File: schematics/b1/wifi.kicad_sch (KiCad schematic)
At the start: 13 parts, among them J1 SERIAL, SW1 JUMP, SW2 RESET, SW3 BOOT, U1 L7805, U2 ESP-12F

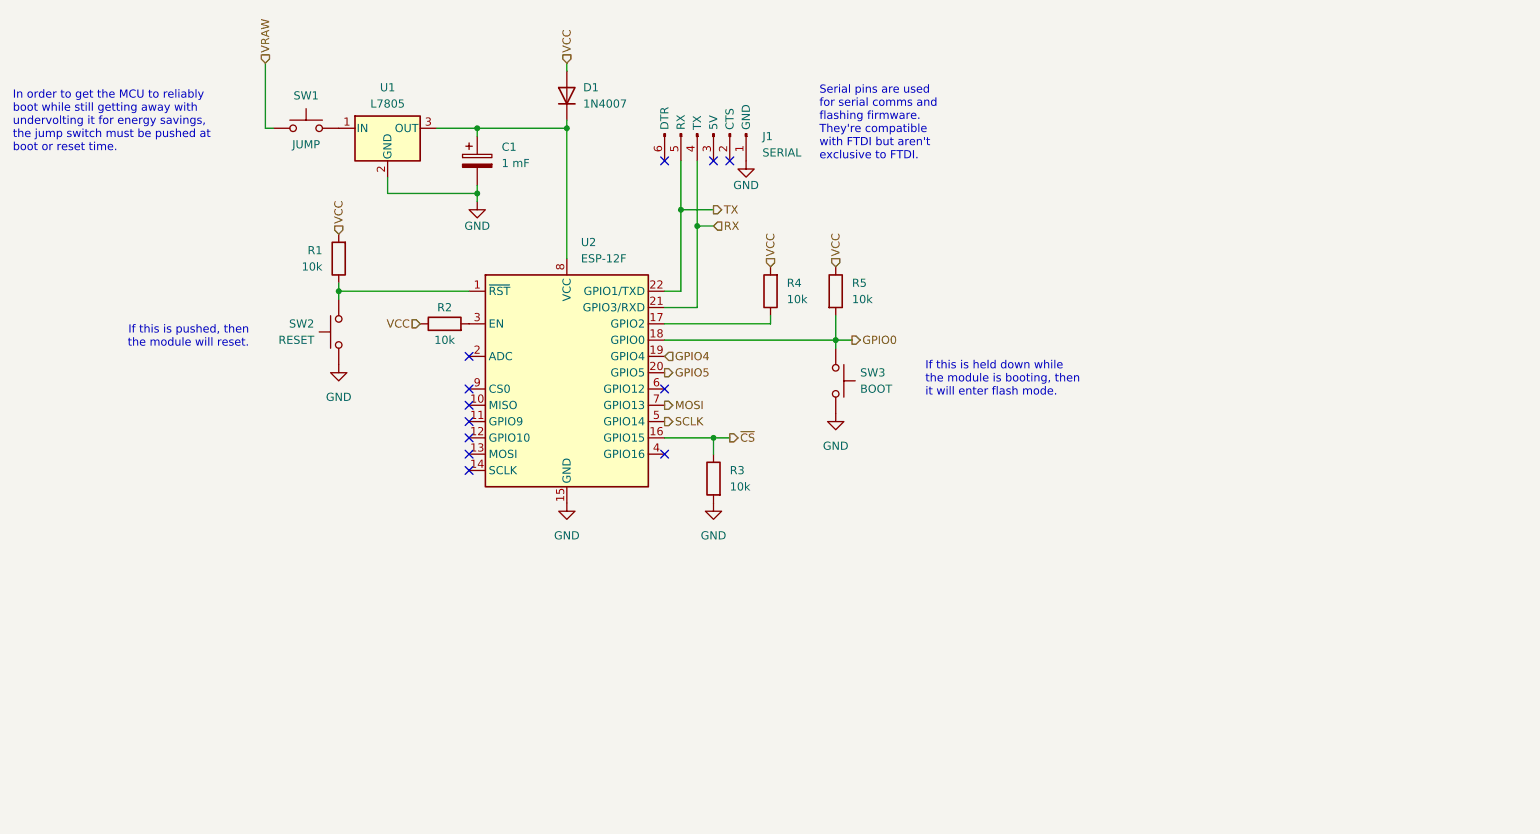
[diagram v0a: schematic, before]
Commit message: Added an MCP23017 IC to the Wi-Fi and MCU block.
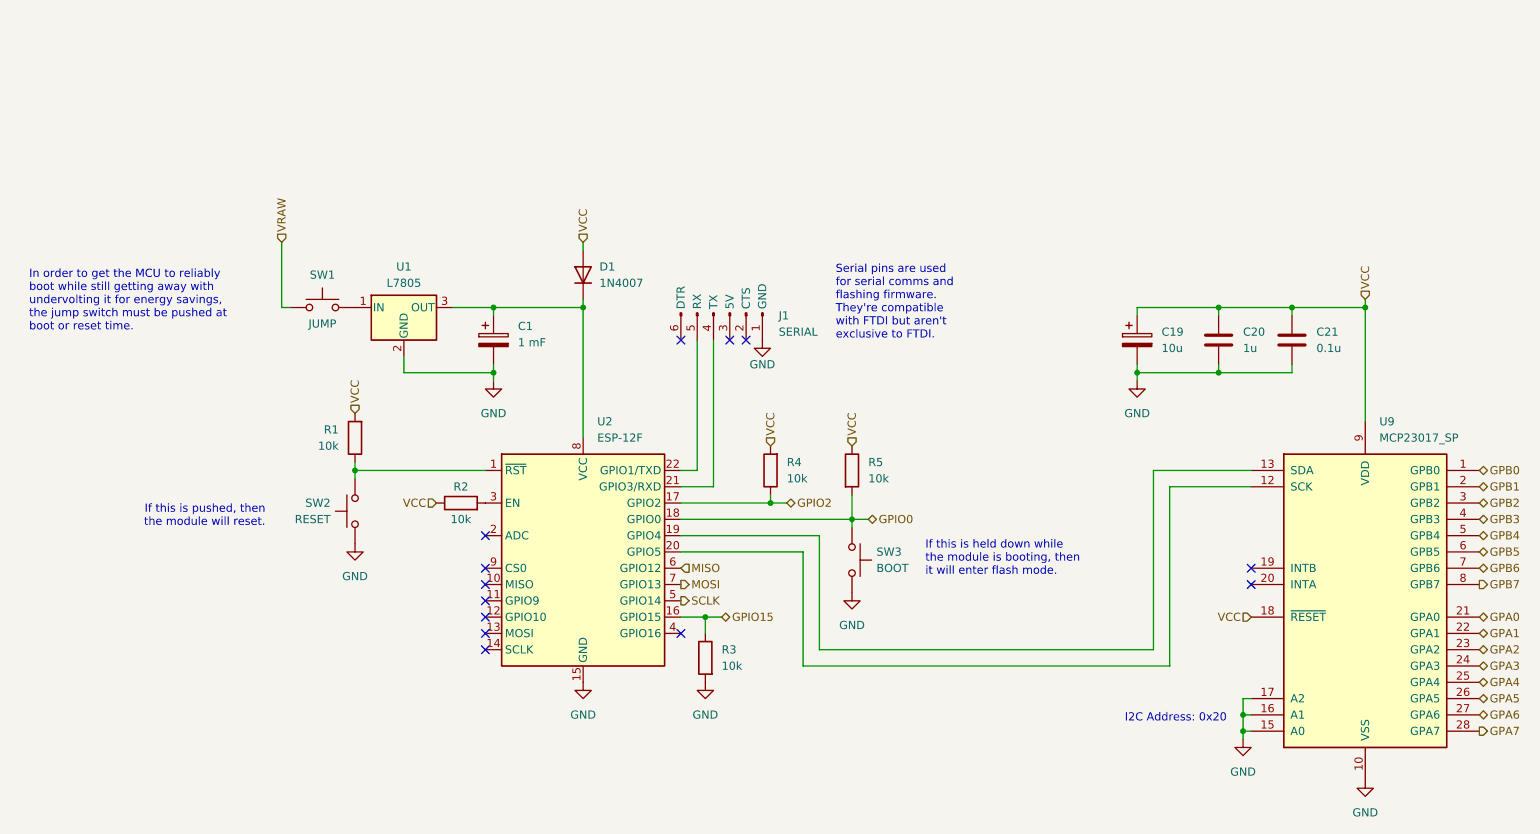
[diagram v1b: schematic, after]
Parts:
- added C19: 10u, symbol Device:C_Polarized
- added C20: 1u, symbol Device:C
- added C21: 0.1u, symbol Device:C
- added U9: MCP23017_SP, Package_DIP:DIP-28_W7.62mm, symbol Interface_Expansion:MCP23017_SP
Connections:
- net GND: now also C19.2, C20.2, C21.2, U9.10 (VSS), U9.15 (A0), U9.16 (A1), U9.17 (A2)
- net VCC: now also C19.1, C20.1, C21.1, U9.18 (~{RESET}), U9.9 (VDD)
- net GPIO2: now reaches R4.1, U2.17 (GPIO2)
- net MISO: now reaches U2.6 (GPIO12)
- net GPIO4: no longer names the net of U2.19 (GPIO4)
- net GPIO4: now also U9.13 (SDA)
- net GPIO5: no longer names the net of U2.20 (GPIO5)
- net GPIO5: now also U9.12 (SCK)
- net RX: no longer names the net of J1.4 (TX), U2.21 (GPIO3/RXD)
- net TX: no longer names the net of J1.5 (RX), U2.22 (GPIO1/TXD)
- net ~{CS} renamed GPIO15
- new net GPA0: U9.21 (GPA0)
- new net GPA1: U9.22 (GPA1)
- new net GPA2: U9.23 (GPA2)
- new net GPA3: U9.24 (GPA3)
- new net GPA4: U9.25 (GPA4)
- new net GPA5: U9.26 (GPA5)
- new net GPA6: U9.27 (GPA6)
- new net GPA7: U9.28 (GPA7)
- new net GPB0: U9.1 (GPB0)
- new net GPB1: U9.2 (GPB1)
- new net GPB2: U9.3 (GPB2)
- new net GPB3: U9.4 (GPB3)
- new net GPB4: U9.5 (GPB4)
- new net GPB5: U9.6 (GPB5)
- new net GPB6: U9.7 (GPB6)
- new net GPB7: U9.8 (GPB7)
- no-connect marks 12 -> 13
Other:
- note added: "I2C Address: 0x20"
- moved on the sheet: C1, D1, J1, R1, R2, R3, R4, R5, SW1, SW2, SW3, U1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

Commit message: Redid general format and MCU wiring.
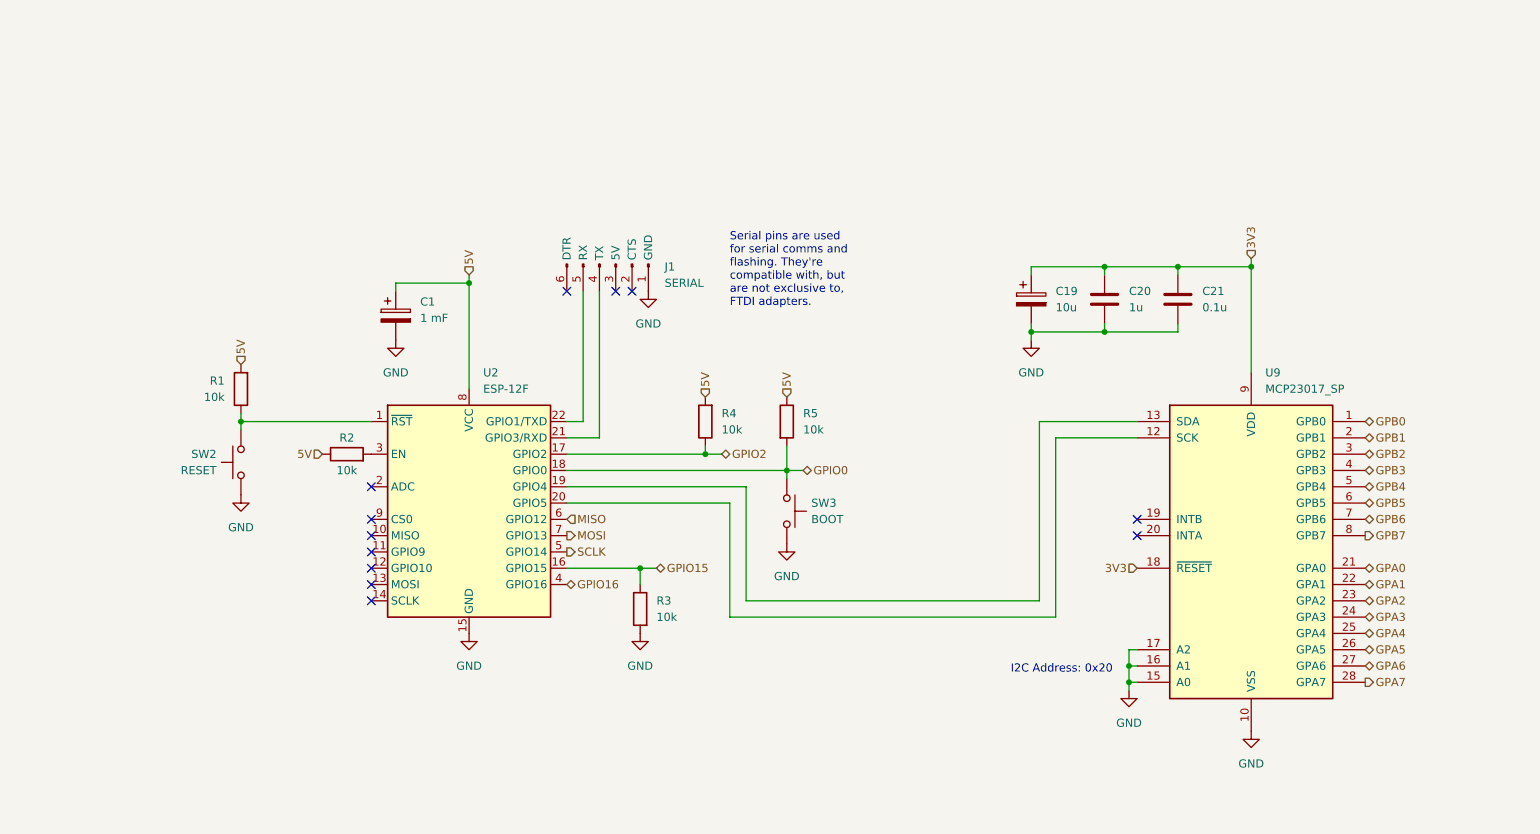
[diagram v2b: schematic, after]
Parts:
- removed D1: 1N4007, Diode_THT:D_DO-41_SOD81_P10.16mm_Horizontal, symbol Diode:1N4007
- removed SW1: JUMP, symbol Switch:SW_Push
- removed U1: L7805, symbol Regulator_Linear:L7805
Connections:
- net 5V: now reaches C1.1, U2.8 (VCC)
- net 5V: now also R1.2, R2.1, R4.2, R5.1
- net GPIO16: now reaches U2.4 (GPIO16)
- net VCC renamed 3V3
- net 3V3: no longer R1.2, R2.1, R4.2, R5.1
- no-connect marks 13 -> 12
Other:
- note added: "Serial pins are used for serial comms and flashing. They're compatible with, but are not exclusive to, FTDI adapters."
- note removed: "If this is held down while the module is booting, then it will enter flash mode."
- note removed: "If this is pushed, then the module will reset."
- note removed: "In order to get the MCU to reliably boot while still getting away with undervolting it for energy savings, the jump switch must be pushed at boot or reset time."
- note removed: "Serial pins are used for serial comms and flashing firmware. They're compatible with FTDI but aren't exclusive to FTDI."
- moved on the sheet: C1, C19, C20, C21, J1, R1, R2, R3, R4, R5, SW2, SW3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
